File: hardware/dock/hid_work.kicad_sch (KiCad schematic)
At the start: 15 parts, among them J5 L-KLS1-5416-L1-01-R, J6 Conn_01x05_Pin, U6 TPD4E1U06DBVR

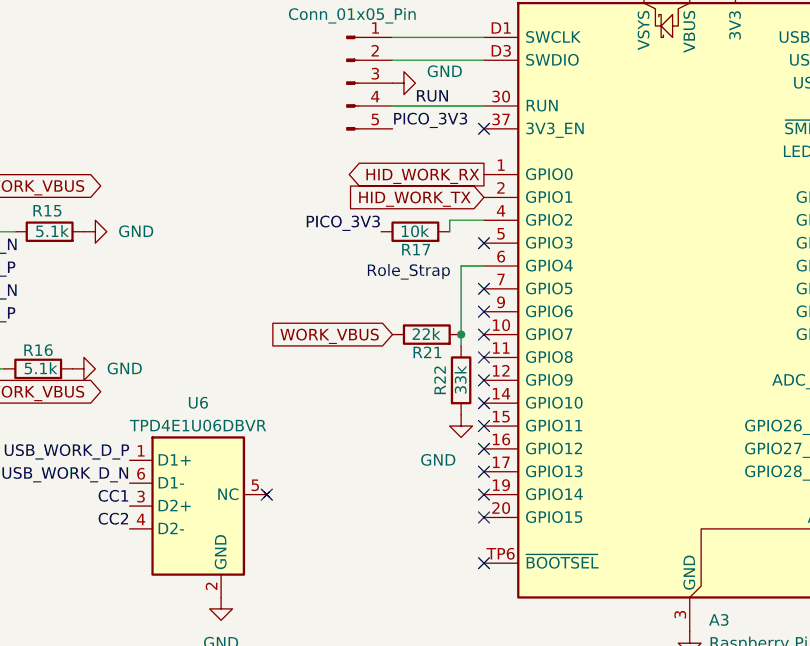
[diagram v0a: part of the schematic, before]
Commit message: Re-pin host/endpoint GPIOs by PCB position; update placement guide
- Host A1: HID-A UART0 -> GP12/13, HID-B UART1 -> GP20/21, BLE PIO ->
  GP16/17, KEYBOARD_VBUS_EN/FAULT -> GP26/27, MUX_STATUS -> GP28,
  POGO_5V_FAULT -> GP18, HID_PERSONAL_RUN_CTRL -> GP2,
  HID_WORK_RUN_CTRL -> GP19 (BLE_RST_CTRL stays GP22)
- HID-A UART0 -> GP16/17, HID-B UART0 -> GP12/13 (pins facing the host)
- Ratsnest crossings on current placement 132 -> 95
- DESIGN.md pin tables updated; PCB_PLACEMENT.md: pull-up/pull-down
  placement, Pico GPIO map, 100x100 outline, routing techniques
- Stop tracking KiCad _restore_backup_* folders (kept on disk, ignored)

Co-Authored-By: Claude Opus 5.5 <noreply@anthropic.com>
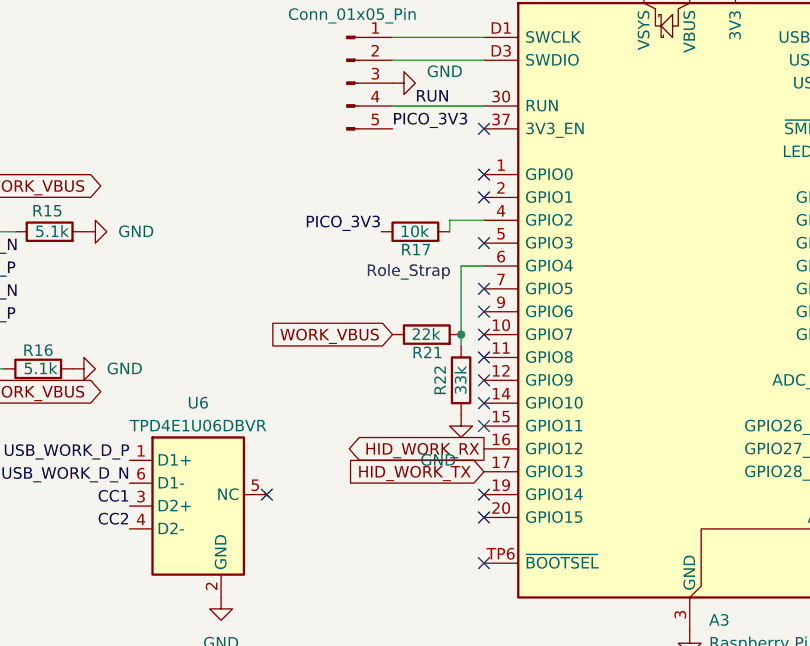
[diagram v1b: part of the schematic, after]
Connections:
- net HID_WORK_RX: now also A3.16 (GPIO12); no longer A3.1 (GPIO0)
- net HID_WORK_TX: now also A3.17 (GPIO13); no longer A3.2 (GPIO1)
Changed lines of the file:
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@@
-	)
-	(no_connect
-		(at 133.35 116.84)
 	)
 	(no_connect
 		(at 133.35 129.54)
-	)
-	(no_connect
-		(at 133.35 119.38)
 	)
 	(no_connect
@@
 		)
 	)
-	(global_label "HID_WORK_RX"
-		(shape output)
-		(at 133.35 86.36 180)
-		(fields_autoplaced yes)
-		(effects
-			(font
-				(size 1.27 1.27)
-			)
-			(justify right)
-		)
-		(property "Intersheetrefs" "${INTERSHEET_REFS}"
-			(at 117.7253 86.36 0)
-			(hide yes)
-			(show_name no)
-			(do_not_autoplace no)
-			(effects
-				(font
-					(size 1.27 1.27)
-				)
-				(justify right)
-			)
-		)
-	)
 	(global_label "WORK_VBUS"
 		(shape input)
@@
 				)
 				(justify left)
-			)
-		)
-	)
-	(global_label "HID_WORK_TX"
-		(shape input)
-		(at 133.35 88.9 180)
-		(fields_autoplaced yes)
-		(effects
-			(font
-				(size 1.27 1.27)
-			)
-			(justify right)
-		)
-		(property "Intersheetrefs" "${INTERSHEET_REFS}"
-			(at 117.4229 88.9 0)
-			(hide yes)
-			(show_name no)
-			(do_not_autoplace no)
-			(effects
-				(font
-					(size 1.27 1.27)
-				)
-				(justify right)
 			)
 		)
@@
 		)
 	)
+	(global_label "HID_WORK_RX"
+		(shape output)
+		(at 133.35 116.84 180)
+		(fields_autoplaced yes)
+		(effects
+			(font
+				(size 1.27 1.27)
+			)
+			(justify right)
+		)
+		(property "Intersheetrefs" "${INTERSHEET_REFS}"
+			(at 133.35 116.84 0)
+			(hide yes)
+			(show_name no)
+			(do_not_autoplace no)
+			(effects
+				(font
+					(size 1.27 1.27)
+				)
+				(justify right)
+			)
+		)
+	)
+	(global_label "HID_WORK_TX"
+		(shape input)
+		(at 133.35 119.38 180)
+		(fields_autoplaced yes)
+		(effects
+			(font
+				(size 1.27 1.27)
+			)
+			(justify right)
+		)
+		(property "Intersheetrefs" "${INTERSHEET_REFS}"
+			(at 133.35 119.38 0)
+			(hide yes)
+			(show_name no)
+			(do_not_autoplace no)
+			(effects
+				(font
+					(size 1.27 1.27)
+				)
+				(justify right)
+			)
+		)
+	)
+	(no_connect
+		(at 133.35 88.9)
+	)
+	(no_connect
+		(at 133.35 86.36)
+	)
 )
